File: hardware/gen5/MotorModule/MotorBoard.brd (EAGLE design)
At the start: 61 x 50.1 mm, 42 parts, among them J1 M20X2SHROUDED

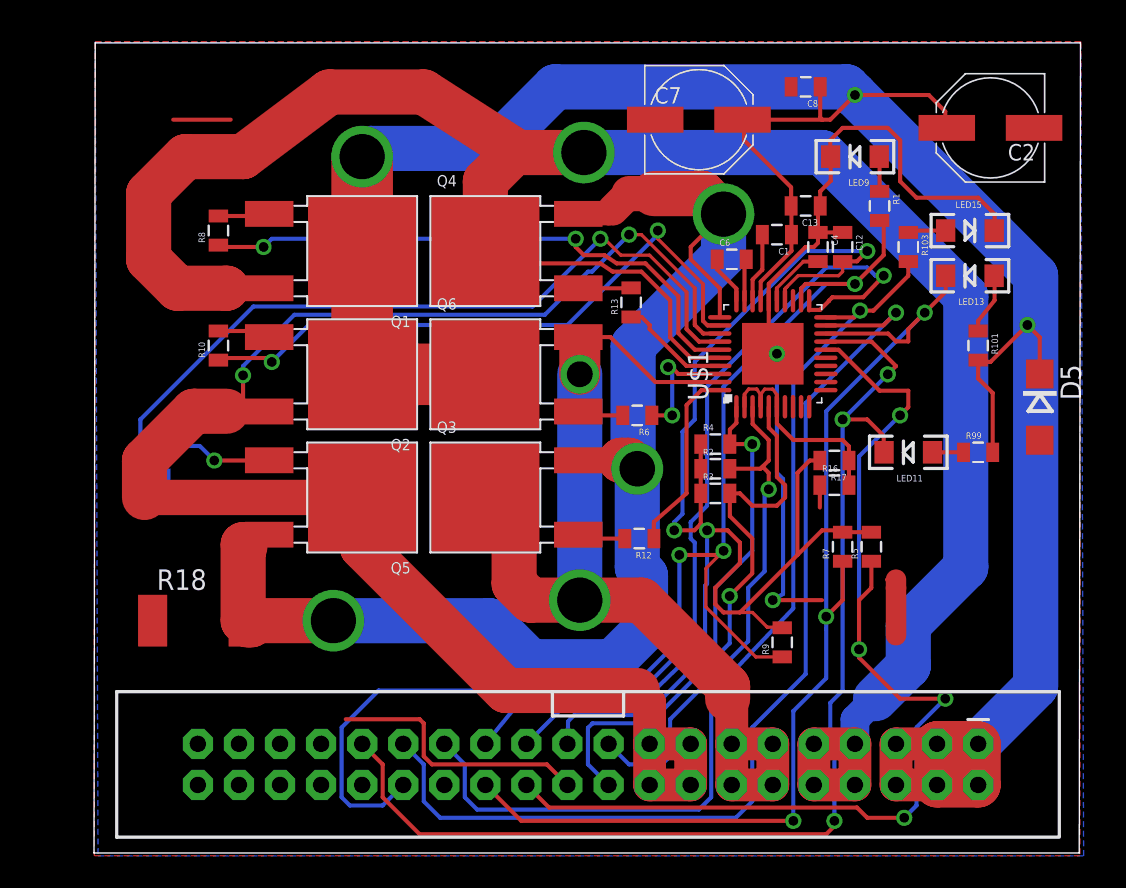
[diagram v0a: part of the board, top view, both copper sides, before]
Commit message: starting to re-write motorboard
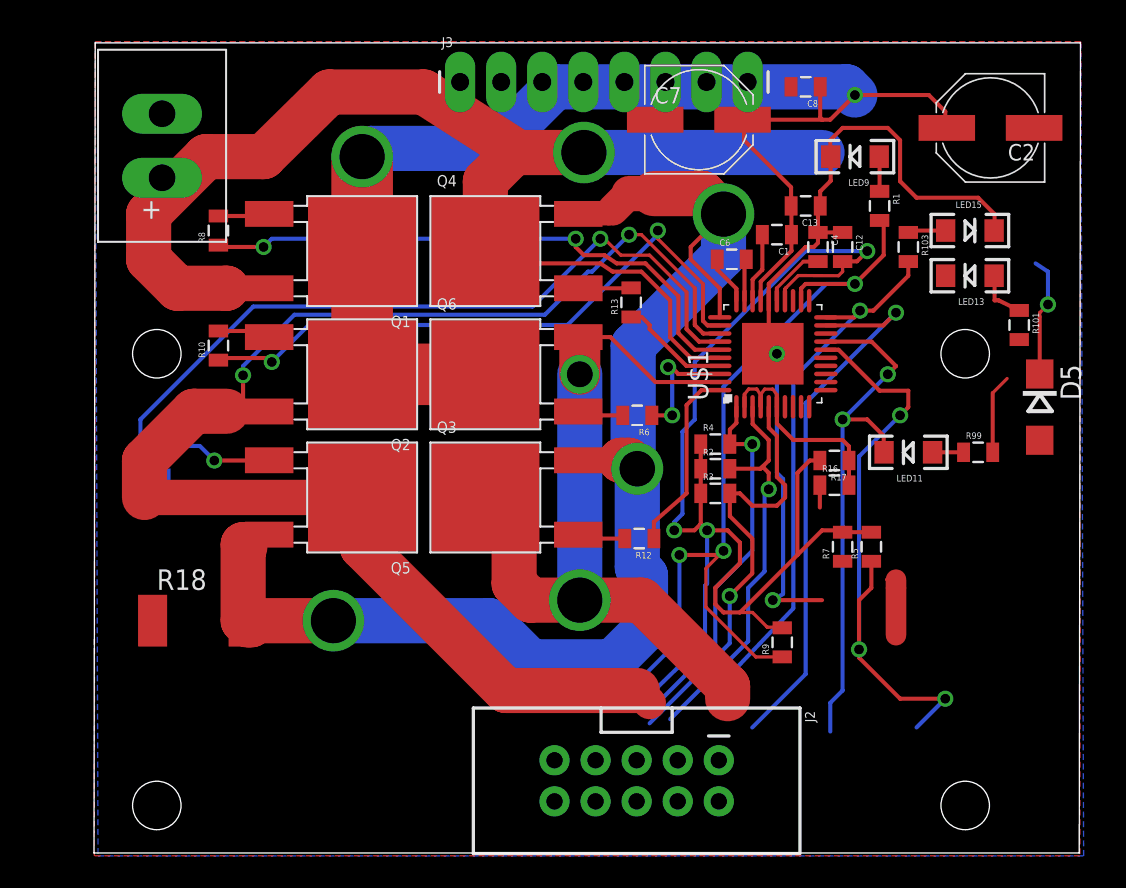
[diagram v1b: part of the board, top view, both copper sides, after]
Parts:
- removed J1: M20X2SHROUDED, SparkFun-Connectors:2X20_SHROUDED
- added J2: (no value), SparkFun-Connectors:2X5-SHROUDED
- added J3: (no value), SparkFun-Connectors:1X08_LONGPADS
- added U$2: CONN-POWER, Kicker:CONN-POWER
- moved R101 2.84 mm to (57.1, 32.3)
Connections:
- new net MO13: J3.3
- net 12V: now also U$2.+; no longer J1.1, J1.2, J1.3, J1.4, J1.5, J1.6
- net 5V: now also J3.4; no longer J1.23
- net BRAKE: now also J2.2; no longer J1.27
- net DIR: now also J2.9; no longer J1.25
- net ENABLE: no longer J1.30
- net FAULTN: now also J2.6; no longer J1.31
- net GND: now also J2.1, J3.5, U$2.-; no longer J1.22, J1.33, J1.34, J1.35, J1.36, J1.37, J1.38, J1.39, J1.40
- net HALLOUT: now also J2.8; no longer J1.24
- net LOCKN: now also J2.10; no longer J1.26
- net M1H1: now also J2.3, J3.6; no longer J1.20
- net M1H2: now also J2.5, J3.7; no longer J1.19
- net M1H3: now also J2.7, J3.8; no longer J1.21
- net M1O1: now also J3.1; no longer J1.11, J1.12, J1.13, J1.14
- net M1O2: now also J3.2; no longer J1.10, J1.7, J1.8, J1.9
- net M1O3: no longer J1.15, J1.16, J1.17, J1.18
- net PWM: now also J2.4; no longer J1.29
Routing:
- net 12V: track 166.4 -> 95.9 mm
- net LOCKN: track 68.9 -> 0.00 mm, vias 3 -> 0
- net M1O2: track 136.2 -> 82.5 mm
- net DIR: track 51.6 -> 0.00 mm, vias 1 -> 0
- net FAULTN: track 72.1 -> 33.2 mm, vias 3 -> 2
- net HALLOUT: track 68.7 -> 38.6 mm, vias 4 -> 3
- net PWM: track 63.8 -> 34.0 mm
- net ENABLE: track 79.9 -> 52.3 mm
- net BRAKE: track 60.6 -> 34.5 mm
- net GND: track 77.3 -> 57.1 mm
- net M1O1: track 61.9 -> 49.2 mm
- net M1O3: track 101.8 -> 89.1 mm
- net M1H1: track 35.6 -> 27.6 mm
- net 5V: track 88.2 -> 80.4 mm
- net M1H2: track 31.5 -> 24.7 mm
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
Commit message: added power connector to library and motorboard
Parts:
- removed U$2: CONN-POWER, Kicker:CONN-POWER
- added U$3: POWER_CONN_2X1, Kicker:POWER_CONN_2X1
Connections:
- net 12V: now also U$3.+; no longer U$2.+
- net GND: now also U$3.-; no longer U$2.-
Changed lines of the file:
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@@
 <element name="R7" library="SparkFun-Resistors" package="0805" value="10k" x="46.228" y="18.542" rot="R90"/>
 <element name="R9" library="SparkFun-Resistors" package="0805" value="0" x="42.49169375" y="12.629140625" rot="R90"/>
-<element name="U$2" library="Kicker" package="CONN-POWER" value="CONN-POWER" x="4.134253125" y="41.363815625" rot="R180"/>
 <element name="J2" library="SparkFun-Connectors" library_urn="urn:adsk.eagle:library:513" package="2X5-SHROUDED" package3d_urn="urn:adsk.eagle:package:38000/1" value="" x="33.48886875" y="4.06571875" rot="R270">
 <attribute name="PROD_ID" value="CONN-08671" x="33.48886875" y="4.06571875" size="1.778" layer="27" rot="R270" display="off"/>
@@
 </element>
 <element name="J3" library="SparkFun-Connectors" library_urn="urn:adsk.eagle:library:513" package="1X08_LONGPADS" package3d_urn="urn:adsk.eagle:package:38142/1" value="" x="22.57101875" y="47.288175"/>
+<element name="U$3" library="Kicker" package="POWER_CONN_2X1" value="POWER_CONN_2X1" x="-112.395" y="10.16"/>
 </elements>
 <signals>
@@
 <vertex x="60.90315" y="-0.568725"/>
 </polygon>
-<contactref element="U$2" pad="-"/>
 <contactref element="J2" pad="1"/>
 <contactref element="J3" pad="5"/>
-<wire x1="34.638" y1="44.958" x2="32.73101875" y2="47.288175" width="0" layer="19" extent="1-1"/>
-<wire x1="4.134253125" y1="45.323815625" x2="32.73101875" y2="47.288175" width="0" layer="19" extent="1-1"/>
+<contactref element="U$3" pad="-"/>
+<wire x1="3.55" y1="13.97" x2="-112.395" y2="6.2" width="0" layer="19" extent="1-1"/>
+<wire x1="38.56886875" y1="5.33571875" x2="3.55" y2="13.97" width="0" layer="19" extent="1-1"/>
+<wire x1="41.91" y1="15.24" x2="38.56886875" y2="5.33571875" width="0" layer="19" extent="16-16"/>
+<wire x1="44.82" y1="22.352" x2="42.545" y2="22.733" width="0" layer="19" extent="1-16"/>
+<wire x1="43.042" y1="46.99" x2="46.228" y2="44.45" width="0" layer="19" extent="1-1"/>
+<wire x1="48.971" y1="16.51" x2="44.958" y2="15.24" width="0" layer="19" extent="1-1"/>
+<wire x1="58.072" y1="44.45" x2="54.61" y2="40.132" width="0" layer="19" extent="1-1"/>
+<wire x1="34.638" y1="44.958" x2="43.042" y2="46.99" width="0" layer="19" extent="1-1"/>
+<wire x1="32.73101875" y1="47.288175" x2="34.638" y2="44.958" width="0" layer="19" extent="1-1"/>
+<wire x1="58.42" y1="25.128" x2="49.53" y2="16.51" width="0" layer="19" extent="1-1"/>
 </signal>
 <signal name="12V">
@@
 <wire x1="55.51" y1="28.056" x2="55.51" y2="24.384" width="0.254" layer="1"/>
 <wire x1="41.16" y1="33.759" x2="41.16" y2="34.937" width="0.254" layer="1"/>
-<contactref element="U$2" pad="+"/>
 <wire x1="56.4022" y1="28.9482" x2="55.51" y2="28.056" width="0.2032" layer="1"/>
 <wire x1="58.42" y1="32.766" x2="58.42" y2="33.02" width="0.2032" layer="1"/>
 <wire x1="58.42" y1="33.02" x2="58.928" y2="33.528" width="0.2032" layer="1"/>
+<contactref element="U$3" pad="+"/>
+<wire x1="16.51" y1="29.21" x2="-112.395" y2="10.16" width="0" layer="19" extent="1-1"/>
+<wire x1="58.166" y1="36.068" x2="52.672" y2="44.45" width="0" layer="19" extent="1-16"/>
 <wire x1="57.15" y1="31.358" x2="58.42" y2="32.766" width="0" layer="19" extent="1-1"/>
 <wire x1="56.4022" y1="28.9482" x2="58.42" y2="29.228" width="0" layer="19" extent="1-1"/>
-<wire x1="52.672" y1="44.45" x2="58.166" y2="36.068" width="0" layer="19" extent="1-16"/>
-<wire x1="4.134253125" y1="41.363815625" x2="16.51" y2="42.672" width="0" layer="19" extent="16-16"/>
 </signal>
 <signal name="M1O1">

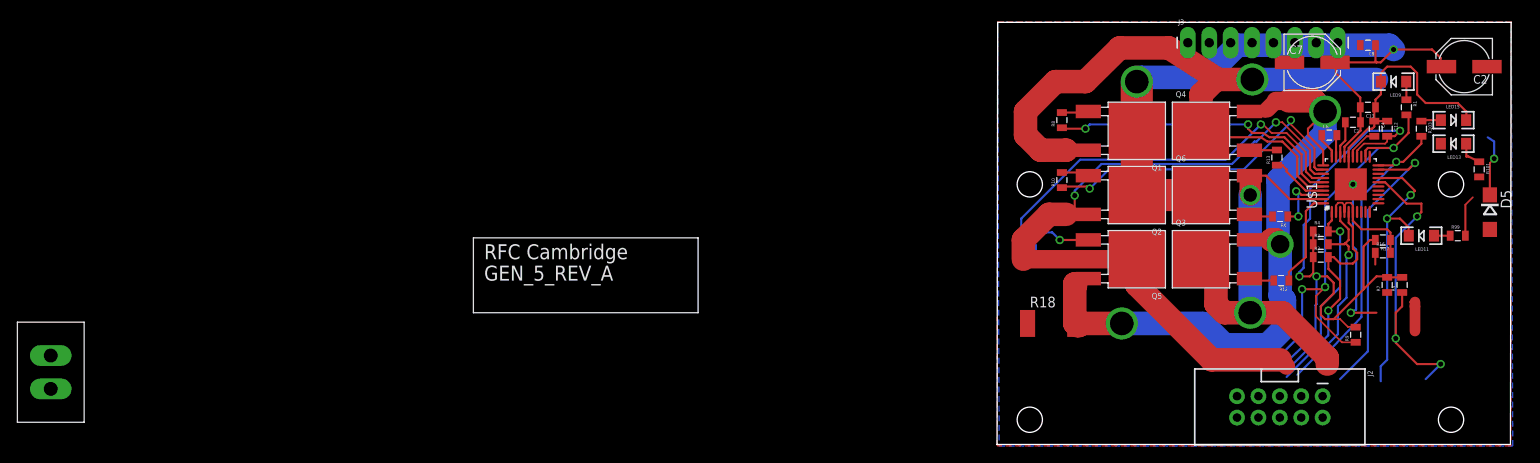
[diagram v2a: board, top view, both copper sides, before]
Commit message: placement ok - started rrouting
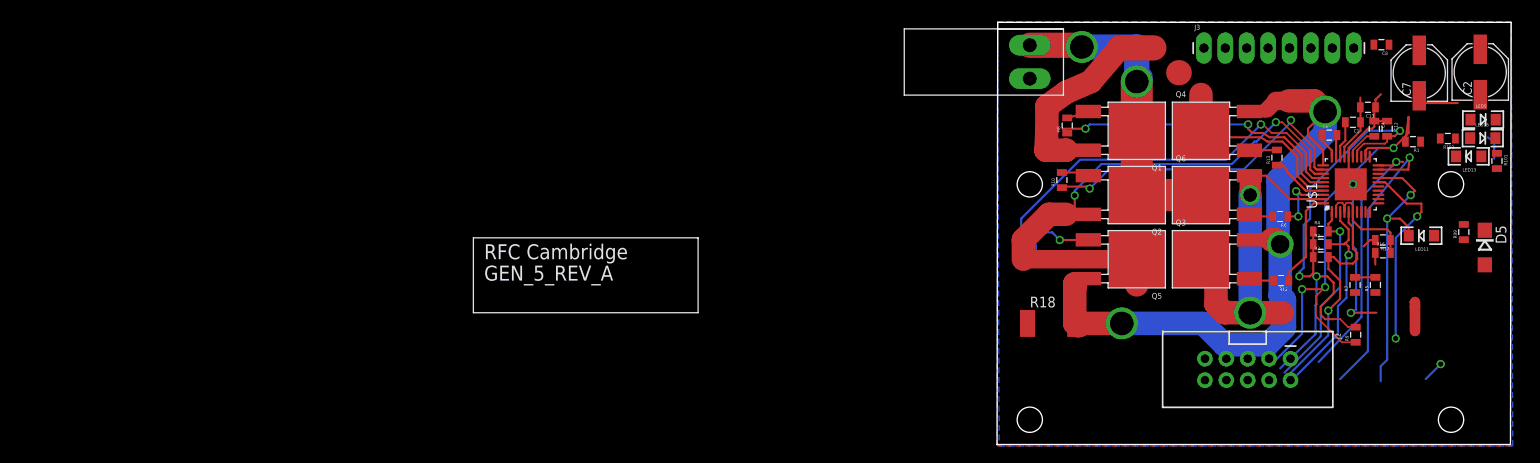
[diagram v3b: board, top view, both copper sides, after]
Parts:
- removed U$3: POWER_CONN_2X1, Kicker:POWER_CONN_2X1
- added U$2: POWER_CONN_2X1, Kicker:POWER_CONN_2X1
- moved C7 12.8 mm to (50.0, 43.7), turned to 90 degrees
- moved LED9 11.5 mm to (57.6, 38.2), turned to 0 degrees
- moved J2 5.85 mm to (29.7, 8.51)
- moved D5 4.24 mm to (57.8, 23.0)
- moved R1 4.15 mm to (49.3, 35.5), turned to 180 degrees
- moved LED15 4.08 mm to (57.6, 36.0)
- moved R7 3.81 mm to (42.4, 18.5)
- moved R103 3.35 mm to (53.4, 35.9), turned to 180 degrees
- moved R5 3.17 mm to (44.8, 18.5)
- moved LED13 2.34 mm to (55.9, 33.8)
- moved R101 2.33 mm to (59.3, 33.3)
- moved C2 2.01 mm to (57.3, 43.8), turned to 90 degrees
- moved J3 2.01 mm to (24.5, 46.7)
- moved C8 1.61 mm to (45.5, 47.1)
- moved R8 0.90 mm to (8.26, 37.5)
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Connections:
- net 12V: now also U$2.+; no longer U$3.+
- net GND: now also U$2.-; no longer U$3.-
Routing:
- net 12V: track 95.9 -> 49.8 mm, vias 3 -> 2
- net M1O2: track 82.5 -> 48.5 mm, vias 1 -> 0
- net M1O3: track 89.1 -> 67.3 mm
- net 5V: track 80.4 -> 67.5 mm
- net HALLOUT: track 38.6 -> 25.9 mm
- net GND: track 57.1 -> 44.6 mm
- net M1O1: track 49.2 -> 40.6 mm
- net BRAKE: track 34.5 -> 30.6 mm
- net N$117: track 3.20 -> 0.00 mm
- net ENABLE: track 52.3 -> 54.9 mm
- net N$119: track 2.36 -> 0.00 mm
- net N$1: track 2.16 -> 0.00 mm
- net N$114: track 1.92 -> 0.00 mm
- net N$20: track 35.9 -> 36.5 mm
- net N$7: track 3.19 -> 2.64 mm

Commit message: lol
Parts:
- moved J2 0.90 mm to (29.7, 7.61)
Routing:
- net M1O2: track 48.5 -> 63.1 mm
- net M1H1: track 27.6 -> 22.9 mm
- net M1H3: track 23.4 -> 18.7 mm
- net M1H2: track 24.7 -> 20.8 mm
- net 5V: track 67.5 -> 63.7 mm
- net ENABLE: track 54.9 -> 51.9 mm
- net BRAKE: track 30.6 -> 28.9 mm
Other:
- board size 61 x 50.1 mm -> 61 x 47.7 mm

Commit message: routed, needs cleanup
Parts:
- moved J2 22.0 mm to (51.0, 13.3)
- moved R9 3.82 mm to (39.8, 15.3)
- moved R5 1.70 mm to (46.0, 19.7)
- moved R7 1.50 mm to (43.3, 19.7)
- moved LED11 0.60 mm to (50.9, 24.4)
- moved U$2 0.28 mm to (3.61, 47.2)
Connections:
- net BRAKE: now also J2.6; no longer J2.2
- net DIR: now also J2.4; no longer J2.9
- net ENABLE: now also J2.8
- net FAULTN: now also J2.10; no longer J2.6
- net HALLOUT: now also J2.9; no longer J2.8
- net LOCKN: now also J2.2; no longer J2.10
- net M1H1: no longer J2.3
- net M1H2: no longer J2.5
- net M1H3: no longer J2.7
- net PWM: now also J2.7; no longer J2.4
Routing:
- net LOCKN: track 0.00 -> 46.7 mm, vias 0 -> 4
- net DIR: track 0.00 -> 38.1 mm, vias 0 -> 2
- net 12V: track 49.8 -> 15.3 mm, vias 2 -> 0
- net GND: track 44.6 -> 22.5 mm, vias 2 -> 4
- net M1H3: track 18.7 -> 40.6 mm, vias 1 -> 4
- net M1H1: track 22.9 -> 38.8 mm, vias 1 -> 2
- net PWM: track 34.4 -> 21.0 mm, vias 1 -> 2
- net M1H2: track 20.8 -> 32.8 mm
- net M1O2: track 63.1 -> 53.0 mm, vias 0 -> 2
- net FAULTN: track 33.2 -> 26.0 mm, vias 2 -> 0
- net N$1: track 0.00 -> 7.15 mm
- net ENABLE: track 51.9 -> 45.7 mm, vias 3 -> 2
- net 5V: track 63.7 -> 69.9 mm
- net HALLOUT: track 25.9 -> 20.6 mm, vias 3 -> 0
- net N$20: track 36.5 -> 41.6 mm, vias 2 -> 1
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- added copper zone on layer 1, net 12V
- removed copper zone on layer 1, net GND

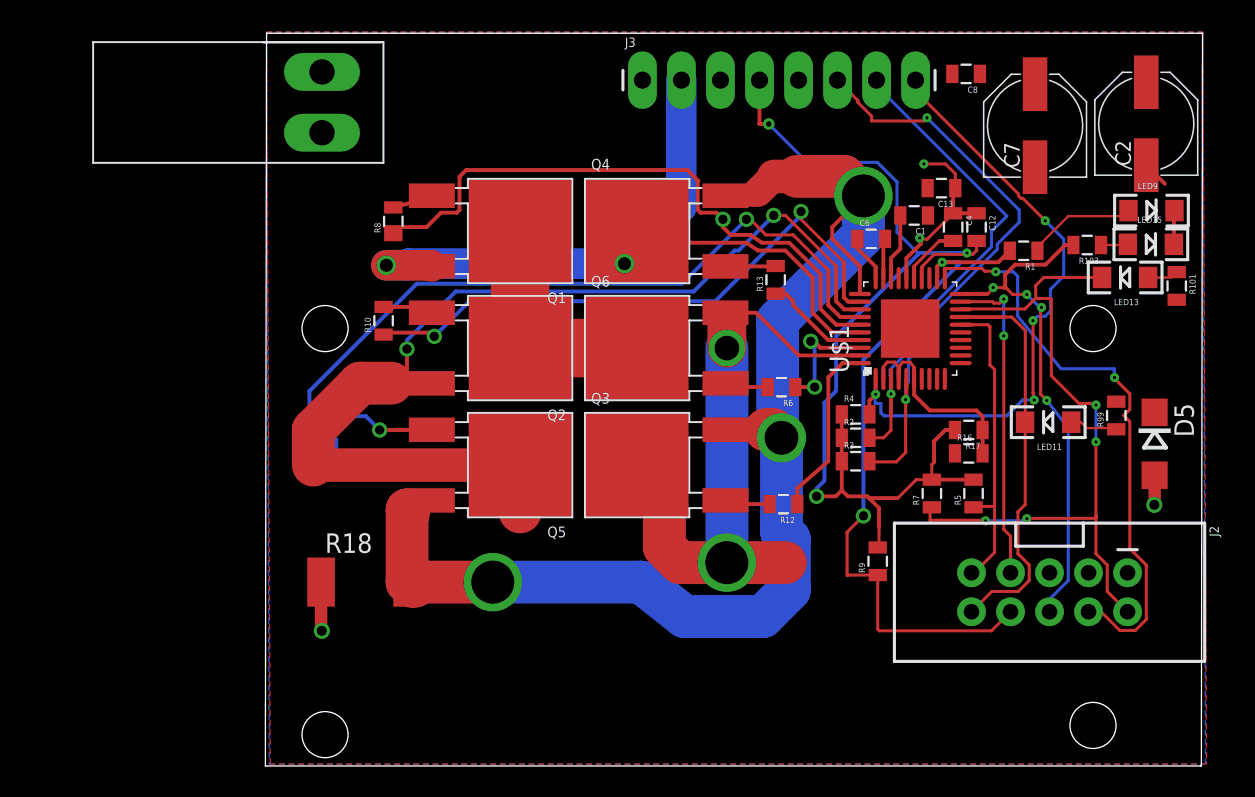
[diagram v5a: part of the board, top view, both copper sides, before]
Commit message: redesigned motorboard 30~ traces to go
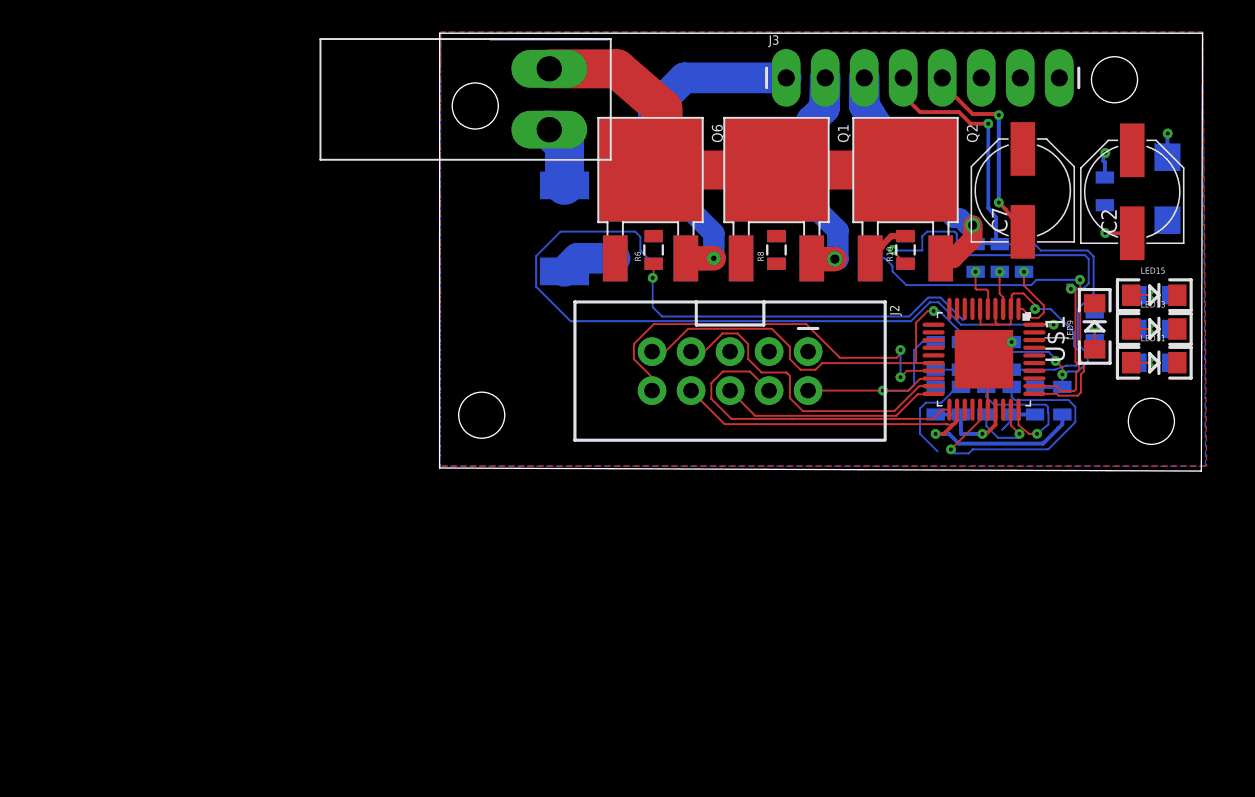
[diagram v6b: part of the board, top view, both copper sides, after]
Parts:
- moved R14 39.3 mm to (41.6, 35.6)
- moved R10 34.3 mm to (41.6, 35.6)
- moved Q5 31.6 mm to (41.6, 40.8), flipped to the bottom, turned to 270 degrees
- moved Q2 27.6 mm to (41.6, 40.8), turned to 270 degrees
- moved R18 26.5 mm to (19.4, 37.0), flipped to the bottom, turned to 270 degrees
- moved J2 25.3 mm to (30.2, 27.7)
- moved R8 25.0 mm to (33.2, 35.6)
- moved Q3 19.2 mm to (25.0, 40.8), flipped to the bottom, turned to 270 degrees
- moved R12 18.6 mm to (25.2, 35.6), flipped to the bottom, turned to 90 degrees
- moved Q1 17.2 mm to (33.2, 40.8), turned to 270 degrees
- moved D5 16.6 mm to (58.7, 39.6), flipped to the bottom
- moved R9 15.9 mm to (51.8, 25.8), flipped to the bottom
- moved R3 15.4 mm to (46.2, 35.1), flipped to the bottom, turned to 270 degrees
- moved R2 15.0 mm to (47.7, 35.1), flipped to the bottom, turned to 270 degrees
- moved R4 15.0 mm to (49.3, 35.1), flipped to the bottom, turned to 270 degrees
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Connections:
- removed net MO13: J3.3
- net M1O3: now also J3.3
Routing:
- net O1: track 83.9 -> 29.1 mm, vias 3 -> 1
- net M1O3: track 67.3 -> 16.1 mm, vias 2 -> 1
- net N$17: track 48.8 -> 0.00 mm, vias 1 -> 0
- net N$20: track 41.6 -> 0.00 mm, vias 1 -> 0
- net M1O2: track 53.0 -> 13.6 mm, vias 2 -> 1
- net N$19: track 11.6 -> 49.4 mm, vias 0 -> 1
- net M1H1: track 38.8 -> 3.14 mm, vias 2 -> 1
- net M1H3: track 40.6 -> 5.22 mm, vias 4 -> 1
- net LOCKN: track 46.7 -> 14.6 mm, vias 4 -> 1
- net M1H2: track 32.8 -> 2.51 mm
- net 12V: track 15.3 -> 39.4 mm, vias 0 -> 3
- net 5V: track 69.9 -> 46.9 mm
- net BRAKE: track 33.8 -> 14.5 mm, vias 4 -> 0
- net M1O1: track 40.6 -> 22.7 mm, vias 2 -> 1
- net N$16: track 7.73 -> 24.4 mm, vias 2 -> 1
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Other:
- board size 61 x 47.7 mm -> 49.7 x 28.5 mm

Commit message: more routing nearly there
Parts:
- moved LED9 0.38 mm to (54.3, 30.6)
- moved R1 0.38 mm to (54.3, 30.6)
- moved R10 0.25 mm to (41.3, 35.6)
- moved R14 0.25 mm to (41.3, 35.6)
- moved R13 0.13 mm to (33.1, 35.6)
- moved R8 0.13 mm to (33.1, 35.6)
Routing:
- net N$20: track 0.00 -> 42.1 mm, vias 0 -> 2
- net M1O1: track 22.7 -> 52.1 mm, vias 1 -> 3
- net GND: track 25.0 -> 52.4 mm, vias 4 -> 6
- net N$18: track 0.00 -> 26.5 mm, vias 0 -> 1
- net M1O2: track 13.6 -> 38.5 mm, vias 1 -> 3
- net O1: track 29.1 -> 53.3 mm
- net N$16: track 24.4 -> 35.0 mm, vias 1 -> 2
- net N$4: track 6.52 -> 13.6 mm, vias 0 -> 1
- net N$14: track 0.00 -> 6.99 mm, vias 0 -> 2
- net N$13: track 0.00 -> 3.84 mm
- net N$11: track 0.00 -> 3.13 mm
- net N$6: track 0.00 -> 3.10 mm
- net N$7: track 0.00 -> 2.77 mm
- net N$22: track 21.3 -> 23.2 mm
- net 5V: track 46.9 -> 48.6 mm
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
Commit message: more routing
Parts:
- turned R10 to 270 degrees
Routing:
- net N$20: track 42.1 -> 35.2 mm
- net N$10: track 2.84 -> 0.07 mm
- net N$21: track 29.9 -> 27.2 mm
- net O1: track 53.3 -> 50.7 mm
- net N$14: track 6.99 -> 6.65 mm, vias 2 -> 0
